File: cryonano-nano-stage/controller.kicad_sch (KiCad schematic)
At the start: 20 parts, among them J8 Conn_ST_STDC14, SW1 BOOT, SW2 RESET, U2 STM32L412CxTx, Y1 32.768kHz, Y2 12.0MHz

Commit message: sch improved
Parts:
- removed C14, C15, C64: 100n, Capacitor_SMD:C_0603_1608Metric, symbol Device:C_Small
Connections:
- net +3V3V: no longer J8.3 (VCC), R35.1, R38.1, U2.24 (VDD_1), U2.48 (VDD_2)
- net GND: no longer C16.2, C17.2, C21.2, C37.2, R36.2, SW2.2
- new net VDD: J8.3 (VCC), R35.1, R38.1
- new net VDD_1: U2.24 (VDD_1)
- new net VDD_2: U2.48 (VDD_2)
- new net VSS: C16.2, C17.2, C21.2, C37.2, R36.2, SW2.2
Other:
- added sheet MCU GPIO A,B,C (mcu-gpio-a-b-c.kicad_sch)
- added sheet MCU GPIO D,E,F,G (mcu-gpio-d-e-f-g.kicad_sch)
- added sheet MCU Power (mcu-power.kicad_sch)
- moved on the sheet: C11, C20, C21, C36, C37, U2A, U2B, Y1, Y2

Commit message: sch improved
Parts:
- removed C16, C17: 100n, Capacitor_SMD:C_0603_1608Metric, symbol Device:C_Small
- removed C20, C21, C36, C37: 22pF, Capacitor_SMD:C_0603_1608Metric, symbol Device:C_Small
- removed R35: 470R, Resistor_SMD:R_0603_1608Metric, symbol Device:R_Small
- removed R36, R38: 10k, Resistor_SMD:R_0603_1608Metric, symbol Device:R_Small
- removed SW1: BOOT, Button_Switch_THT:SW_PUSH_6mm, symbol Switch:SW_Push
- removed SW2: RESET, Button_Switch_THT:SW_PUSH_6mm, symbol Switch:SW_Push
- removed U2: STM32L412CxTx, QFP50P900X900X160-48N, symbol symbols:STM32L412CxTx
- removed Y1: 32.768kHz, Crystal:Crystal_SMD_3215-2Pin_3.2x1.5mm, symbol Device:Crystal
- removed Y2: 12.0MHz, Crystal:Crystal_SMD_3215-2Pin_3.2x1.5mm, symbol Device:Crystal
- added R91: 100R, Resistor_SMD:R_0603_1608Metric, symbol Device:R_Small
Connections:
- net +3V3V is gone; now on net VDD: C11.1, FB3.2
- net GND: now also R91.2; no longer J8.11 (GNDDetect)
- new net GNDDETECT: J8.11 (GNDDetect), R91.1
- no-connect marks 3 -> 2
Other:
- sheet MCU GPIO A,B,C renamed MCU GPIO
- removed sheet MCU GPIO D,E,F,G
- sheet MCU GPIO: file mcu-gpio-a-b-c.kicad_sch -> mcu-gpio.kicad_sch
- sheet MCU GPIO ports: added CLKOUT, LOG_RX, LOG_TX, NRST, PWMOUT, RMII_CRS_DV, RMII_MDC, RMII_MDIO, RMII_REF_CLK, RMII_RXD0, RMII_RXD1, RMII_TXD0, RMII_TXD1, RMII_TX_EN, SCK, SDI, SDO/~{IRQ}, SWCLK, SWDIO, SWO, USB_D+, USB_D-, USB_ID, USB_VBUS_SENSE, VDD, VSS, ~{CS}, ~{SYNC}; removed none
- sheet MCU Power ports: added VDD, VSS; removed none
- note removed: "BOOT memory selection."
- note removed: "MCU reset."
- note removed: "Power conditioning."
- note removed: "SIGNALS"
- moved on the sheet: C11, FB3, J8

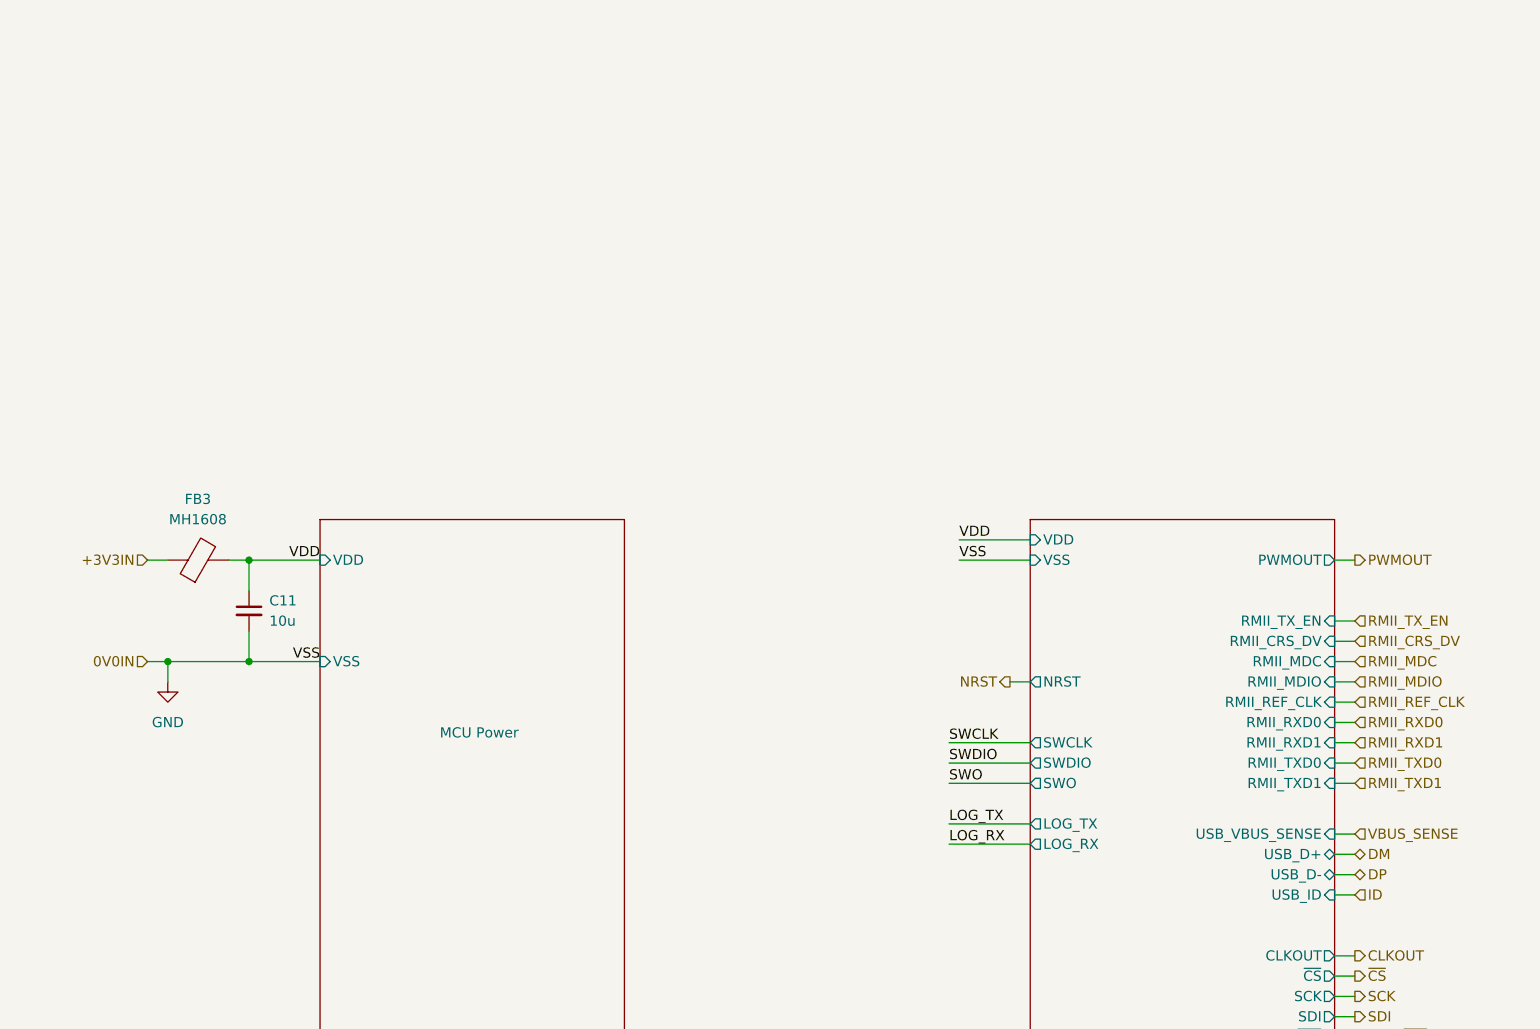
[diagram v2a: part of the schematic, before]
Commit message: pcb drc ok. 68 ohm matching pending
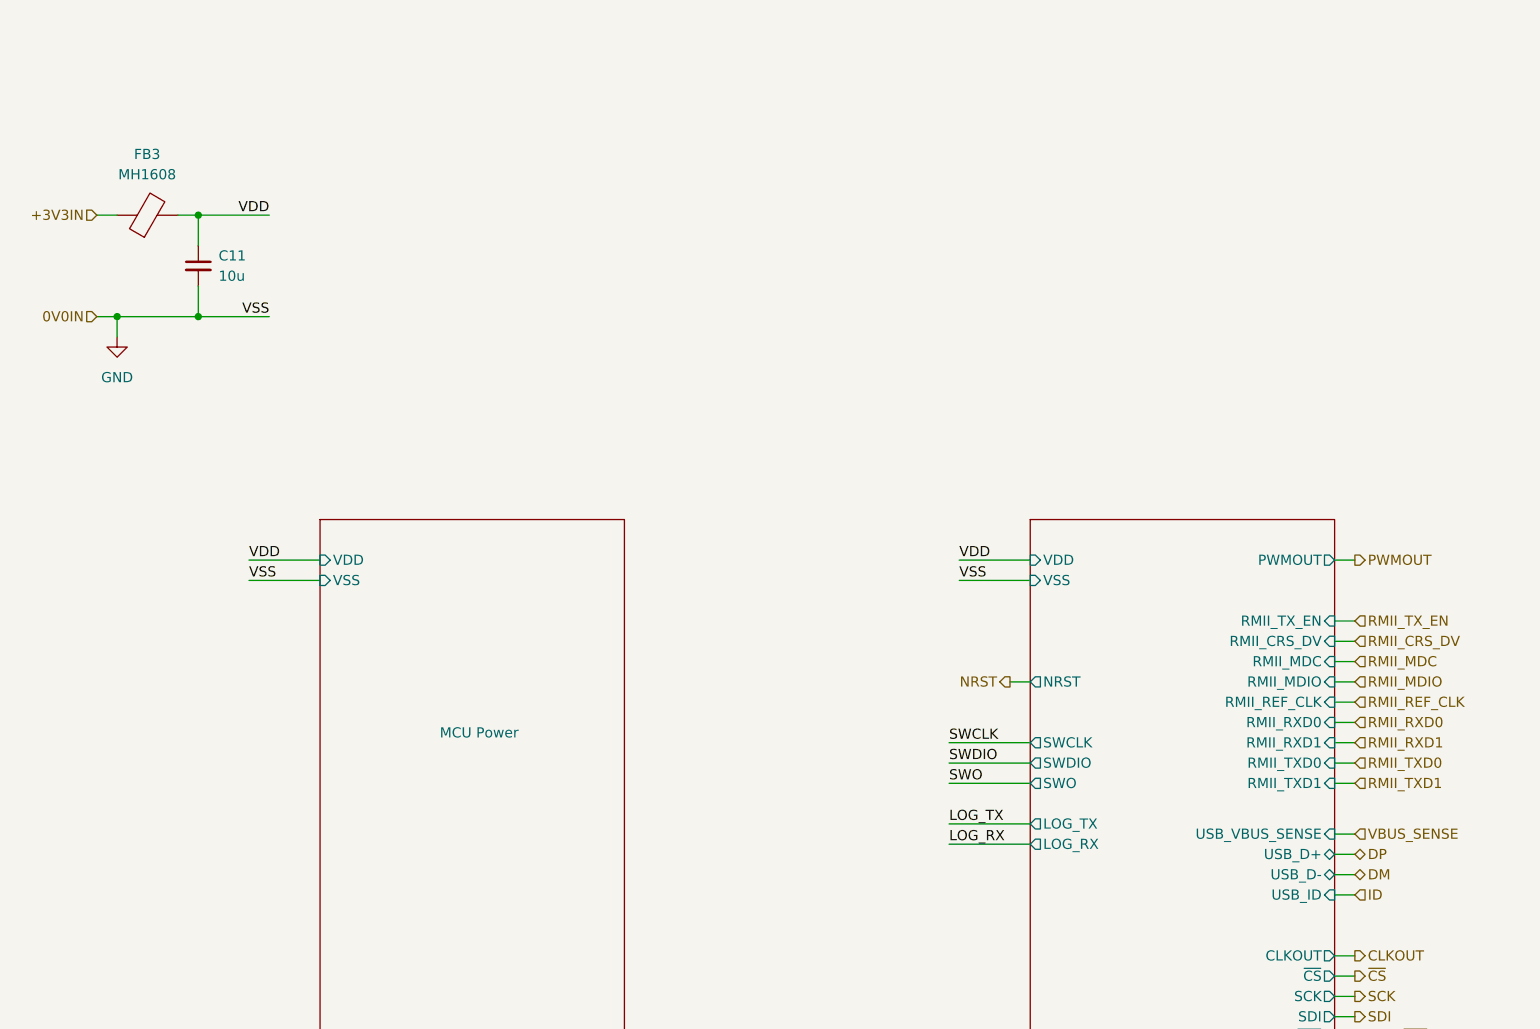
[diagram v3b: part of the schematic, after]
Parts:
- C11: footprint Capacitor_SMD:C_0805_2012Metric -> Capacitor_SMD:C_1206_3216Metric; Manufacturer (none) -> KEMET; Order No. (none) -> C1206C106K4RACTU; Unit Price 10 (none) -> 13.5
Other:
- moved on the sheet: C11, FB3

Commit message: bom adjusted
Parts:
- J8: Order No. (none) -> 2x07, 2.54mm pitch
- R91: Order No. (none) -> 0603/120mW
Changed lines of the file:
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@@
+			)
+		)
+		(property "Order No." "2x07, 2.54mm pitch"
+			(at 251.46 129.54 0)
+			(hide yes)
+			(show_name no)
+			(do_not_autoplace no)
+			(effects
+				(font
+					(size 1.27 1.27)
+				)
 			)
 		)
@@
 			)
 		)
-		(property "Order No." ""
+		(property "Order No." "0603/120mW"
 			(at 231.14 147.32 0)
 			(hide yes)

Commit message: drc ok. chip level review pending
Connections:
- no-connect marks 2 -> 3
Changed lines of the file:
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@@
 		(at 266.7 134.62)
 	)
+	(no_connect
+		(at 177.8 123.19)
+	)
 	(wire
 		(pts
@@
 		(stroke
 			(width 0.1524)
-			(type default)
-		)
-	)
-	(wire
-		(pts
-			(xy 177.8 123.19) (xy 180.34 123.19)
-		)
-		(stroke
-			(width 0)
 			(type default)
 		)
@@
 		)
 	)
-	(hierarchical_label "ID"
-		(shape input)
-		(at 180.34 123.19 0)
-		(effects
-			(font
-				(size 1.27 1.27)
-				(thickness 0.1588)
-			)
-			(justify left)
-		)
-	)

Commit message: release candidate
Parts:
- R91: Order No. 0603/120mW -> 0603, 120mW
